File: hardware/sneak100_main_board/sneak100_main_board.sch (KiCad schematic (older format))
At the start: 0 parts

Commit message: Version 1.1 begin
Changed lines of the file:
@@
 	6400 5550 6900 5550
+Wire Wire Line
+	4900 5150 4450 5150
 Wire Wire Line
 	4900 5250 4450 5250
 Wire Wire Line
-	4900 5350 4450 5350
+	4900 4800 4450 4800
 Wire Wire Line
-	4900 4600 4450 4600
+	4900 4900 4450 4900
 Wire Wire Line
-	4900 4700 4450 4700
-Wire Wire Line
-	4450 4900 4900 4900
+	4450 4500 4900 4500
 Wire Wire Line
 	4450 2450 4900 2450
@@
 F0 "interface" 50
 F1 "interface.sch" 50
-F2 "BLUETOOTH_RX" I R 4450 5250 50
-F3 "BLUETOOTH_TX" O R 4450 5350 50
-F4 "I2C_SDA" B R 4450 4700 50
-F5 "I2C_SCL" B R 4450 4600 50
+F2 "BLUETOOTH_RX" I R 4450 5150 50
+F3 "BLUETOOTH_TX" O R 4450 5250 50
+F4 "I2C_SDA" B R 4450 4000 50
+F5 "I2C_SCL" B R 4450 3900 50
 F6 "RECEIVER_OUT" O R 4450 4900 50
 F7 "BUTTON_L" O R 4450 3600 50
-F8 "LED_RUN" I R 4450 4000 50
-F9 "BUTTON_C" O R 4450 3700 50
-F10 "BUTTON_R" O R 4450 3800 50
-F11 "LED_ERROR" I R 4450 4100 50
-F12 "BLUETOOTH_EN" I R 4450 5450 50
-F13 "BLUETOOTH_STATUS" O R 4450 5550 50
+F8 "BUTTON_C" O R 4450 3700 50
+F9 "BUTTON_R" O R 4450 3800 50
+F10 "BLUETOOTH_EN" I R 4450 5350 50
+F11 "LED_GREEN" I R 4450 4500 50
+F12 "LED_YELLOW" I R 4450 4800 50
+F13 "DEBUG_TX" O R 4450 4400 50
+F14 "DEBUG_RX" I R 4450 4300 50
+F15 "BLUETOOTH_PWR" I R 4450 5550 50
+F16 "BLUETOOTH_ST" O R 4450 5450 50
 $EndSheet
 Wire Wire Line
@@
 	4450 3800 4900 3800
 Wire Wire Line
+	4450 3900 4900 3900
+Wire Wire Line
 	4450 4000 4900 4000
 Wire Wire Line
-	4450 4100 4900 4100
+	4900 5350 4450 5350
 Wire Wire Line
 	4900 5450 4450 5450
-Wire Wire Line
-	4900 5550 4450 5550
 $Sheet
 S 6900 4200 1350 500
@@
 F2 "RF_A" I R 6400 2700 50
 F3 "RF_B" I R 6400 2800 50
-F4 "USART2_TX" O L 4900 5250 50
-F5 "USART2_RX" I L 4900 5350 50
-F6 "LB_A" I R 6400 3200 50
-F7 "LB_B" I R 6400 3300 50
-F8 "I2C3_SCL" B L 4900 4600 50
-F9 "LB_IN1" O R 6400 3000 50
-F10 "LB_IN2" O R 6400 3100 50
-F11 "RB_A" I R 6400 3700 50
-F12 "RB_B" I R 6400 3800 50
-F13 "RB_IN1" O R 6400 3500 50
-F14 "RB_IN2" O R 6400 3600 50
-F15 "RF_IN1" O R 6400 2500 50
-F16 "RF_IN2" O R 6400 2600 50
-F17 "LF_IN1" O R 6400 2000 50
-F18 "LF_IN2" O R 6400 2100 50
-F19 "LINE_LL" I R 6400 5250 50
-F20 "LINE_LM" I R 6400 5350 50
-F21 "LINE_RM" I R 6400 5450 50
-F22 "LINE_RR" I R 6400 5550 50
-F23 "BATTERY_SENSE" I L 4900 2450 50
-F24 "LF_A" I R 6400 2200 50
-F25 "LF_B" I R 6400 2300 50
-F26 "I2C3_SDA" B L 4900 4700 50
-F27 "RECEIVER_OUT" I L 4900 4900 50
-F28 "USER_LED_RUN" O L 4900 4000 50
-F29 "USER_LED_ERROR" O L 4900 4100 50
-F30 "USER_BUTTON_C" I L 4900 3700 50
-F31 "USER_BUTTON_L" I L 4900 3600 50
-F32 "USER_BUTTON_R" I L 4900 3800 50
-F33 "BLUETOOTH_EN" O L 4900 5450 50
-F34 "BLUETOOTH_STATUS" I L 4900 5550 50
-F35 "PROXIMITY_LL" I R 6400 4300 50
-F36 "PROXIMITY_FL" I R 6400 4400 50
-F37 "PROXIMITY_FR" I R 6400 4500 50
-F38 "PROXIMITY_RR" I R 6400 4600 50
+F4 "LB_A" I R 6400 3200 50
+F5 "LB_B" I R 6400 3300 50
+F6 "LB_IN1" O R 6400 3000 50
+F7 "LB_IN2" O R 6400 3100 50
+F8 "RB_A" I R 6400 3700 50
+F9 "RB_B" I R 6400 3800 50
+F10 "RB_IN1" O R 6400 3500 50
+F11 "RB_IN2" O R 6400 3600 50
+F12 "RF_IN1" O R 6400 2500 50
+F13 "RF_IN2" O R 6400 2600 50
+F14 "LF_IN1" O R 6400 2000 50
+F15 "LF_IN2" O R 6400 2100 50
+F16 "LINE_LL" I R 6400 5250 50
+F17 "LINE_LM" I R 6400 5350 50
+F18 "LINE_RM" I R 6400 5450 50
+F19 "LINE_RR" I R 6400 5550 50
+F20 "BATTERY_SENSE" I L 4900 2450 50
+F21 "LF_A" I R 6400 2200 50
+F22 "LF_B" I R 6400 2300 50
+F23 "RECEIVER_OUT" I L 4900 4900 50
+F24 "USER_BUTTON_C" I L 4900 3700 50
+F25 "USER_BUTTON_L" I L 4900 3600 50
+F26 "USER_BUTTON_R" I L 4900 3800 50
+F27 "BLUETOOTH_EN" O L 4900 5350 50
+F28 "PROXIMITY_LL" I R 6400 4300 50
+F29 "PROXIMITY_FL" I R 6400 4400 50
+F30 "PROXIMITY_FR" I R 6400 4500 50
+F31 "PROXIMITY_RR" I R 6400 4600 50
+F32 "USART2_TX" O L 4900 4300 50
+F33 "USART2_RX" I L 4900 4400 50
+F34 "I2C1_SCL" B L 4900 3900 50
+F35 "I2C1_SDA" B L 4900 4000 50
+F36 "USART3_TX" O L 4900 5150 50
+F37 "USART3_RX" I L 4900 5250 50
+F38 "BLUETOOTH_PWR" O L 4900 5550 50
+F39 "USER_LED_GREEN" O L 4900 4500 50
+F40 "USER_LED_YELLOW" O L 4900 4800 50
+F41 "BLUETOOTH_ST" I L 4900 5450 50
 $EndSheet
+Wire Wire Line
+	4900 4300 4450 4300
+Wire Wire Line
+	4900 4400 4450 4400
+Wire Wire Line
+	4900 5550 4450 5550
 $EndSCHEMATC

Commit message: uController routes finish
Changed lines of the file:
@@
 F30 "PROXIMITY_FR" I R 6400 4500 50
 F31 "PROXIMITY_RR" I R 6400 4600 50
-F32 "USART2_TX" O L 4900 4300 50
-F33 "USART2_RX" I L 4900 4400 50
+F32 "USART2_TX" O L 4900 5150 50
+F33 "USART2_RX" I L 4900 5250 50
 F34 "I2C1_SCL" B L 4900 3900 50
 F35 "I2C1_SDA" B L 4900 4000 50
-F36 "USART3_TX" O L 4900 5150 50
-F37 "USART3_RX" I L 4900 5250 50
+F36 "USART3_TX" O L 4900 4400 50
+F37 "USART3_RX" I L 4900 4300 50
 F38 "BLUETOOTH_PWR" O L 4900 5550 50
 F39 "USER_LED_GREEN" O L 4900 4500 50

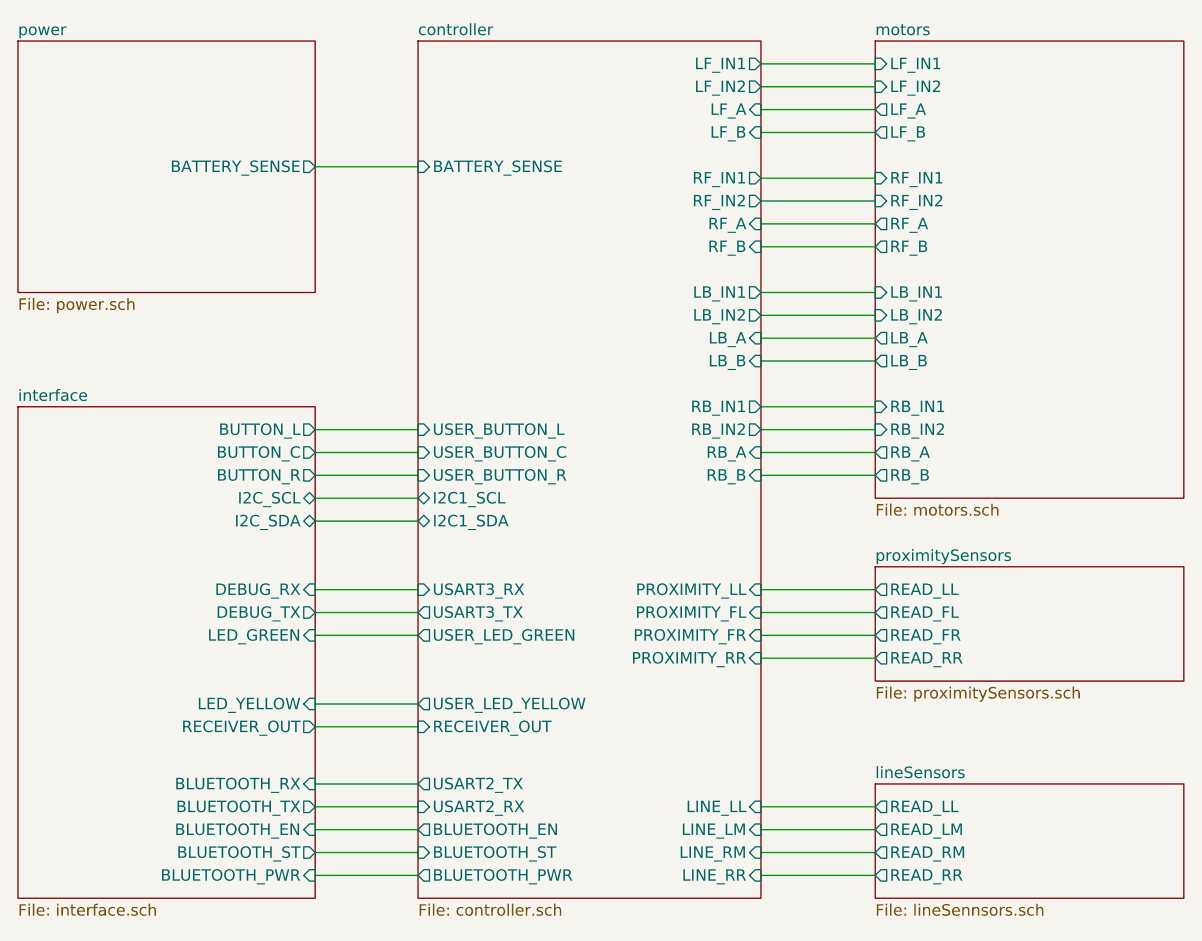
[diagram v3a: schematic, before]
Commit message: Add eeprom chip
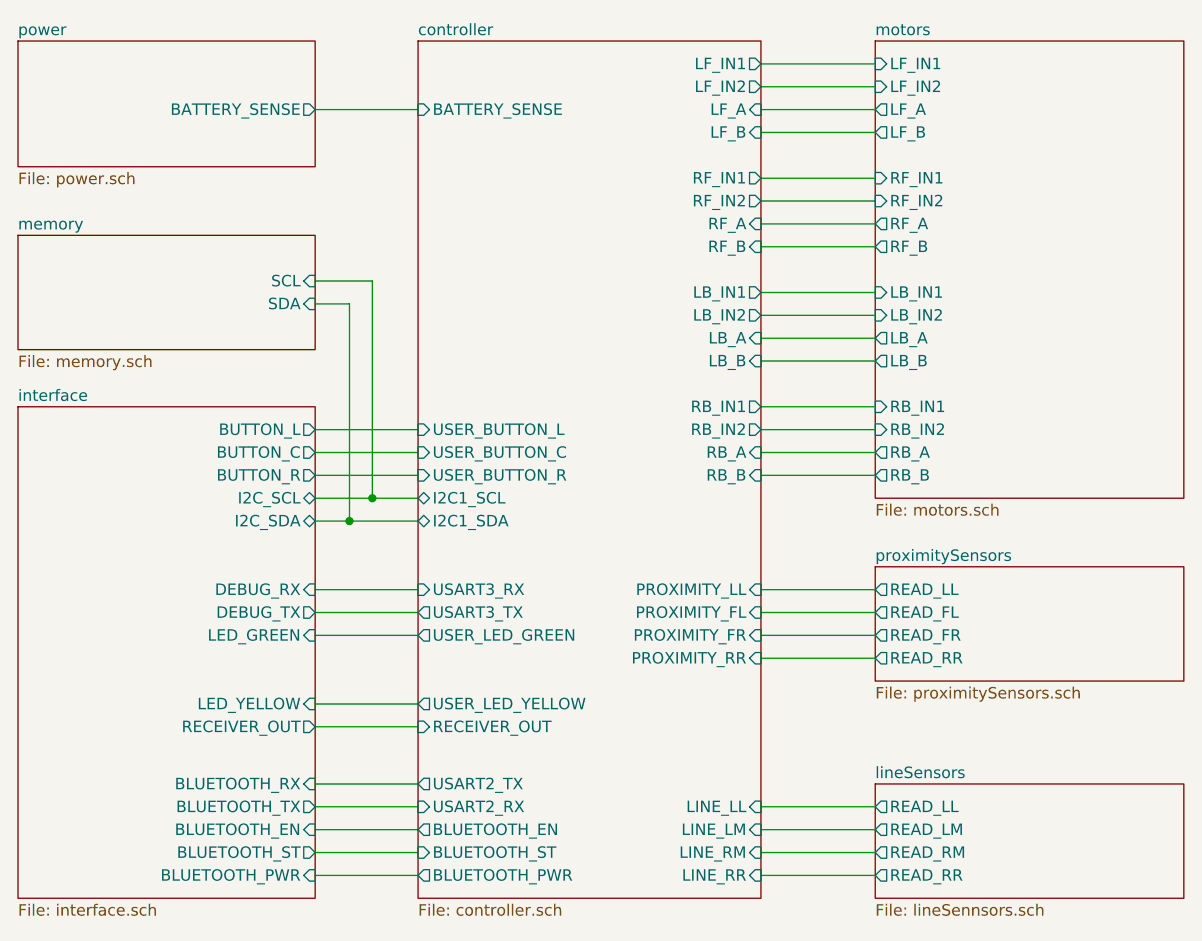
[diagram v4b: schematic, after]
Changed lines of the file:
@@
 $Descr A4 11693 8268
 encoding utf-8
-Sheet 1 7
+Sheet 1 8
 Title "Sneak100 Main Board V1.1"
 Date "September 2021"
@@
 $EndSheet
 $Sheet
-S 3150 1900 1300 1100
-U 60E04AFA
-F0 "power" 50
-F1 "power.sch" 50
-F2 "BATTERY_SENSE" O R 4450 2450 50
-$EndSheet
-$Sheet
 S 6900 5150 1350 500
 U 60E04A74
@@
 	4450 4500 4900 4500
 Wire Wire Line
-	4450 2450 4900 2450
+	4450 2200 4900 2200
 $Sheet
 S 3150 3500 1300 2150
@@
 	4450 3800 4900 3800
 Wire Wire Line
-	4450 3900 4900 3900
-Wire Wire Line
-	4450 4000 4900 4000
+	4450 3900 4700 3900
+Wire Wire Line
+	4450 4000 4600 4000
 Wire Wire Line
 	4900 5350 4450 5350
@@
 F18 "LINE_RM" I R 6400 5450 50
 F19 "LINE_RR" I R 6400 5550 50
-F20 "BATTERY_SENSE" I L 4900 2450 50
+F20 "BATTERY_SENSE" I L 4900 2200 50
 F21 "LF_A" I R 6400 2200 50
 F22 "LF_B" I R 6400 2300 50
@@
 Wire Wire Line
 	4900 5550 4450 5550
+$Sheet
+S 3150 2750 1300 500
+U 61959060
+F0 "memory" 50
+F1 "memory.sch" 50
+F2 "SCL" I R 4450 2950 50
+F3 "SDA" I R 4450 3050 50
+$EndSheet
+$Sheet
+S 3150 1900 1300 550
+U 60E04AFA
+F0 "power" 50
+F1 "power.sch" 50
+F2 "BATTERY_SENSE" O R 4450 2200 50
+$EndSheet
+Wire Wire Line
+	4450 3050 4600 3050
+Wire Wire Line
+	4600 3050 4600 4000
+Connection ~ 4600 4000
+Wire Wire Line
+	4600 4000 4900 4000
+Wire Wire Line
+	4450 2950 4700 2950
+Wire Wire Line
+	4700 2950 4700 3900
+Connection ~ 4700 3900
+Wire Wire Line
+	4700 3900 4900 3900
 $EndSCHEMATC
